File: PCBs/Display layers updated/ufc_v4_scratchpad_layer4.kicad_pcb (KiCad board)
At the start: 2 copper layers, 58 x 16.8 mm, 95 parts

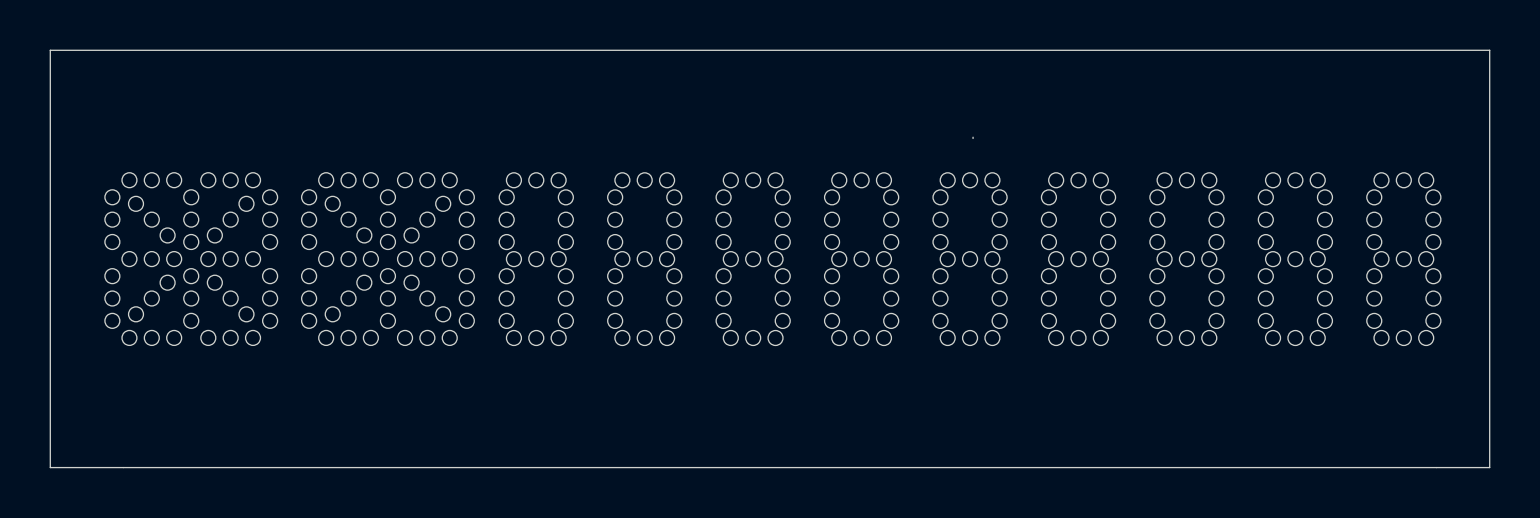
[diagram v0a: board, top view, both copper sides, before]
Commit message: Updated PCBs, cleaned up files
No commit for a while; a lot has happened in the mean time. JLC refused my order for the display layers, so I settled for just the dot layer. The gerbers for the rest are deleted, but the kicad files are still present.

I also received the main PCBs from JLC, and edited a couple small details.
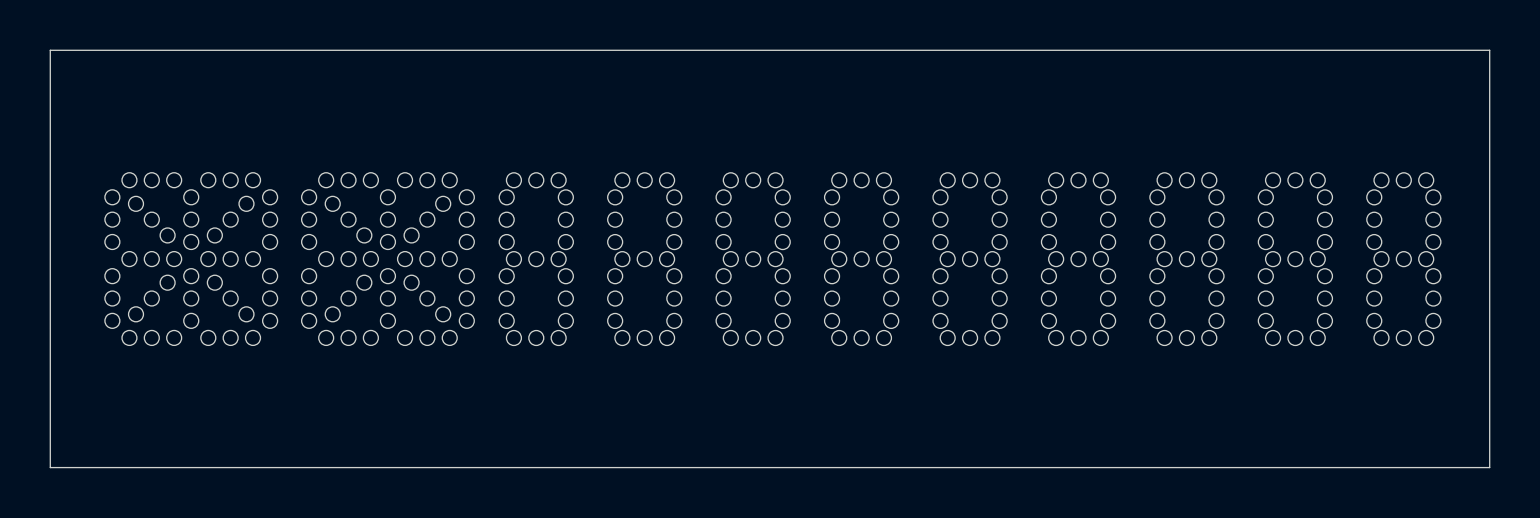
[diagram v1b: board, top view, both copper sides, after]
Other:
- outline, holes or cut-outs redrawn
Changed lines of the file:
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@@
   (general
     (thickness 1.6)
-    (drawings 12)
+    (drawings 9)
     (tracks 0)
     (zones 0)
@@
       (usegerberattributes false)
       (usegerberadvancedattributes false)
-      (creategerberjobfile false)
+      (creategerberjobfile true)
       (excludeedgelayer true)
       (linewidth 0.100000)
@@
       (drillshape 0)
       (scaleselection 1)
-      (outputdirectory "gerber"))
+      (outputdirectory "../Gerbers/Display layers/Scratchpad layer 4/"))
   )
   (net 0 "")
@@
     (pad "" np_thru_hole circle (at 0.9 0) (size 0.6 0.6) (drill 0.6) (layers *.Cu *.Mask))
   )
-  (gr_line (start 197.2125 89.076) (end 144.3625 89.076) (layer Edge.Cuts) (width 0.05))
+  (gr_line (start 199.3625 89.076) (end 141.4125 89.076) (layer Edge.Cuts) (width 0.05))
+  (gr_line (start 199.3625 72.276) (end 199.3625 89.076) (layer Edge.Cuts) (width 0.05))
+  (gr_line (start 141.412 72.276) (end 199.3625 72.276) (layer Edge.Cuts) (width 0.05))
+  (gr_line (start 141.4125 89.076) (end 141.412 72.276) (layer Edge.Cuts) (width 0.05))
   (gr_text "LAYER 4 / TOP LIGHT CHAN\nCC BY-NC-SA" (at 172.0875 73.942) (layer B.SilkS)
     (effects (font (size 0.6 0.6) (thickness 0.15)) (justify mirror))
@@
   (gr_circle (center 147.0875 80.692) (end 147.183221 80.692) (layer Dwgs.User) (width 0.05))
   (gr_circle (center 155.005 80.692) (end 155.100721 80.692) (layer Dwgs.User) (width 0.05))
-  (gr_line (start 141.4125 89.076) (end 144.3625 89.076) (layer Edge.Cuts) (width 0.05))
-  (gr_line (start 141.4125 72.276) (end 141.4125 89.076) (layer Edge.Cuts) (width 0.05))
-  (gr_line (start 141.412 72.276) (end 199.363 72.276) (layer Edge.Cuts) (width 0.05))
-  (gr_line (start 199.3625 89.076) (end 197.2125 89.076) (layer Edge.Cuts) (width 0.05))
-  (gr_line (start 199.3625 72.276) (end 199.3625 89.076) (layer Edge.Cuts) (width 0.05))
-  (gr_line (start 178.5625 75.776) (end 178.5625 75.826) (layer Edge.Cuts) (width 0.05))
   (gr_text "THIS SIDE DOWN" (at 142.5625 80.676 270) (layer B.SilkS)
     (effects (font (size 0.6 0.6) (thickness 0.15)) (justify mirror))
